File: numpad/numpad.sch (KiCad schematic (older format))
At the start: 13 parts, among them SW1 SW_PUSH, U1 ATMEGA32U4, X1 XTAL_GND

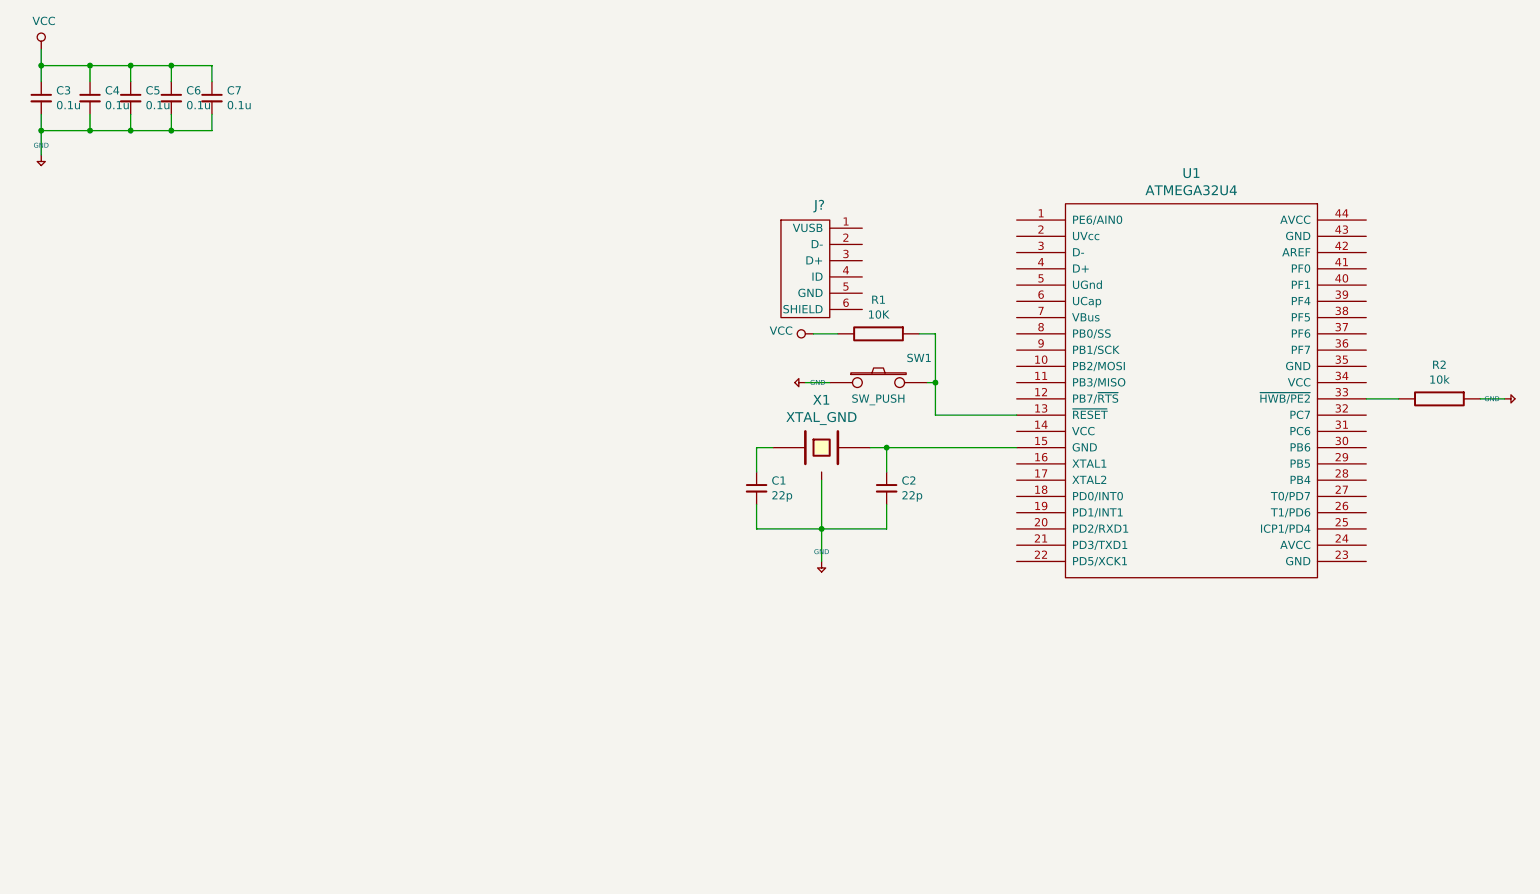
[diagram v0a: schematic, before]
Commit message: finished schematic, associated part to footprints
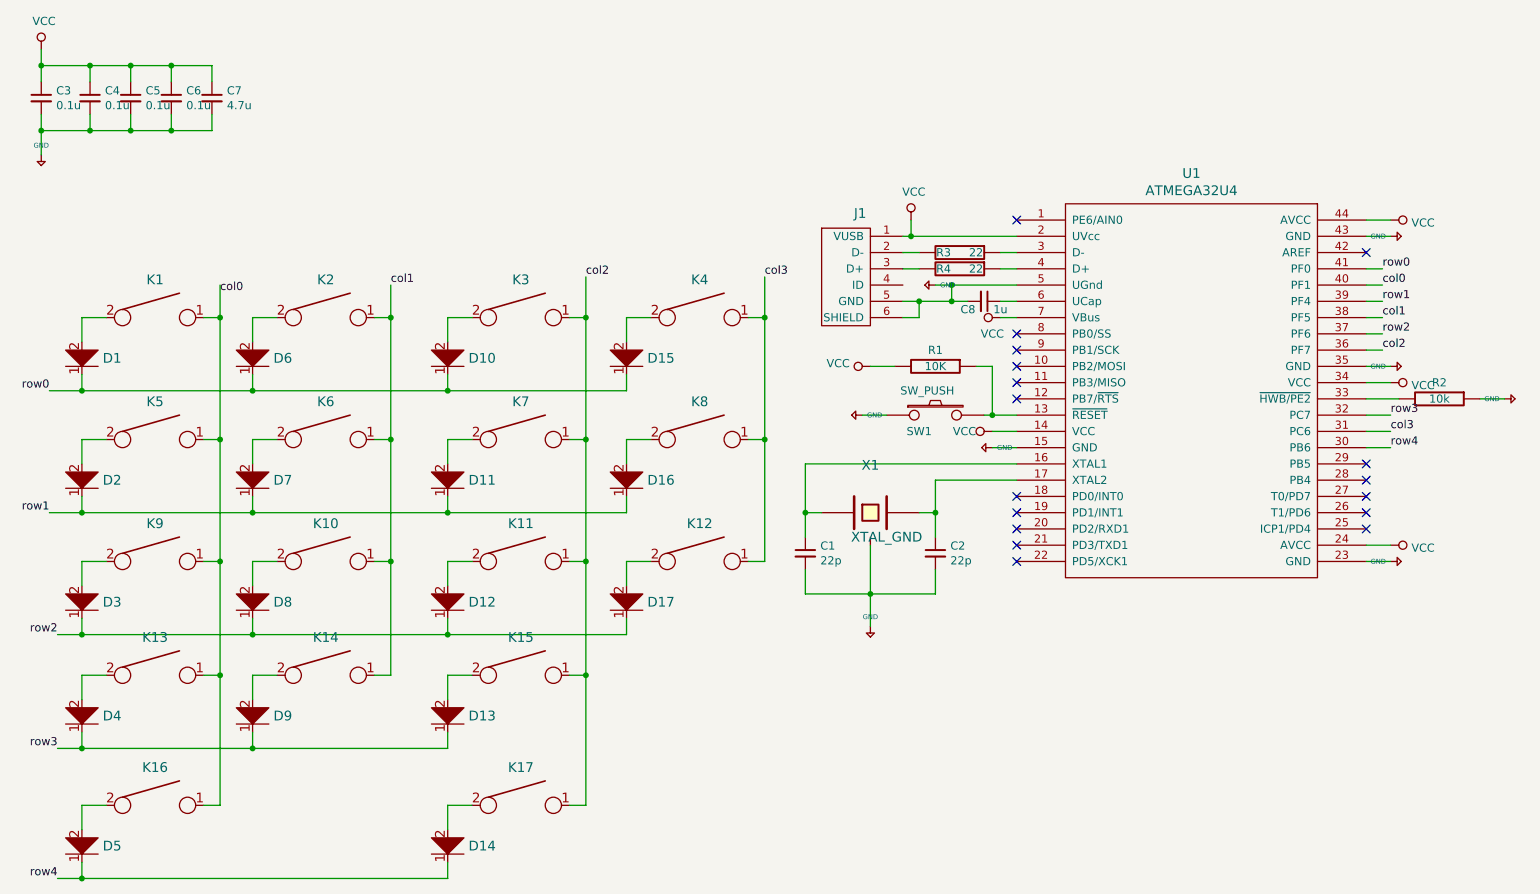
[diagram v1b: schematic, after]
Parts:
- added C8: 1u, Capacitor_SMD:C_0805_2012Metric_Pad1.15x1.40mm_HandSolder, symbol Device:C_Small
- added D1, D10, D11, D12, D13, D14, D15, D16, D17, D2, D3, D4, D5, D6, D7, D8, D9: D, keyboard_parts:D_SOD123_axial, symbol keyboard_parts:D
- added K1, K10, K11, K12, K13, K14, K15, K16, K17, K2, K3, K4, K5, K6, K7, K8, K9: KEYSW, keebs:Mx_Alps_100, symbol keyboard_parts:KEYSW
- added R3, R4: 22, Resistor_SMD:R_0805_2012Metric_Pad1.15x1.40mm_HandSolder, symbol keyboard_parts:R
- C1, C2, C3, C4, C5, C6: footprint (none) -> Capacitor_SMD:C_0805_2012Metric_Pad1.15x1.40mm_HandSolder
- C7: value 0.1u -> 4.7u; footprint (none) -> Capacitor_SMD:C_0805_2012Metric_Pad1.15x1.40mm_HandSolder
- J1: renamed from J?; footprint (none) -> keyboard_parts:USB_miniB_hirose_5S8
- R1, R2: footprint (none) -> Resistor_SMD:R_0805_2012Metric_Pad1.15x1.40mm_HandSolder
- SW1: footprint (none) -> Button_Switch_SMD:SW_SPST_TL3342
- U1: footprint (none) -> Package_QFP:TQFP-44_10x10mm_P0.8mm
- X1: footprint (none) -> Crystal:Crystal_SMD_SeikoEpson_FA238-4Pin_3.2x2.5mm_HandSoldering
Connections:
- net +5V: now also J1.5 (GND), J1.6 (SHIELD), U1.15 (GND), U1.23 (GND), U1.35 (GND), U1.43 (GND), U1.5 (UGnd), C8.2
- net VCC: now also J1.1 (VUSB), U1.14 (VCC), U1.2 (UVcc), U1.24 (AVCC), U1.34 (VCC), U1.44 (AVCC), U1.7 (VBus)
- net at C2.1, X1.3 (2): now also U1.17 (XTAL2); no longer U1.15 (GND)
- net at U1.16 (XTAL1): now also C1.1, X1.1
- net at U1.3 (D-): now also R3.1
- net row4: now reaches U1.30 (PB6)
- net row4: now also D14.1, D5.1
- net col3: now reaches U1.31 (PC6)
- net col3: now also K12.1, K4.1, K8.1
- net row3: now reaches U1.32 (PC7)
- net row3: now also D13.1, D4.1, D9.1
- net col2: now reaches U1.36 (PF7)
- net col2: now also K11.1, K15.1, K17.1, K3.1, K7.1
- net row2: now reaches U1.37 (PF6)
- net row2: now also D12.1, D17.1, D3.1, D8.1
- net col1: now reaches U1.38 (PF5)
- net col1: now also K10.1, K14.1, K2.1, K6.1
- net row1: now reaches U1.39 (PF4)
- net row1: now also D11.1, D16.1, D2.1, D7.1
- net at U1.4 (D+): now also R4.1
- net col0: now reaches U1.40 (PF1)
- net col0: now also K1.1, K13.1, K16.1, K5.1, K9.1
- net row0: now reaches U1.41 (PF0)
- net row0: now also D1.1, D10.1, D15.1, D6.1
- net at U1.6 (UCap): now also C8.1
- net at J1.2 (D-): now also R3.2
- net at J1.3 (D+): now also R4.2
- new net: D1.2, K1.2
- new net: D2.2, K5.2
- new net: D6.2, K2.2
- new net: D7.2, K6.2
- new net: D3.2, K9.2
- new net: D4.2, K13.2
- new net: D5.2, K16.2
- new net: D8.2, K10.2
- new net: D9.2, K14.2
- new net: D10.2, K3.2
- new net: D11.2, K7.2
- new net: D12.2, K11.2
- new net: D13.2, K15.2
- new net: D14.2, K17.2
- new net: D15.2, K4.2
- new net: D16.2, K8.2
- new net: D17.2, K12.2
- no-connect marks 0 -> 17
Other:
- moved on the sheet: C1, C2, J1, R1, SW1, X1

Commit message: finished initial pass on routing
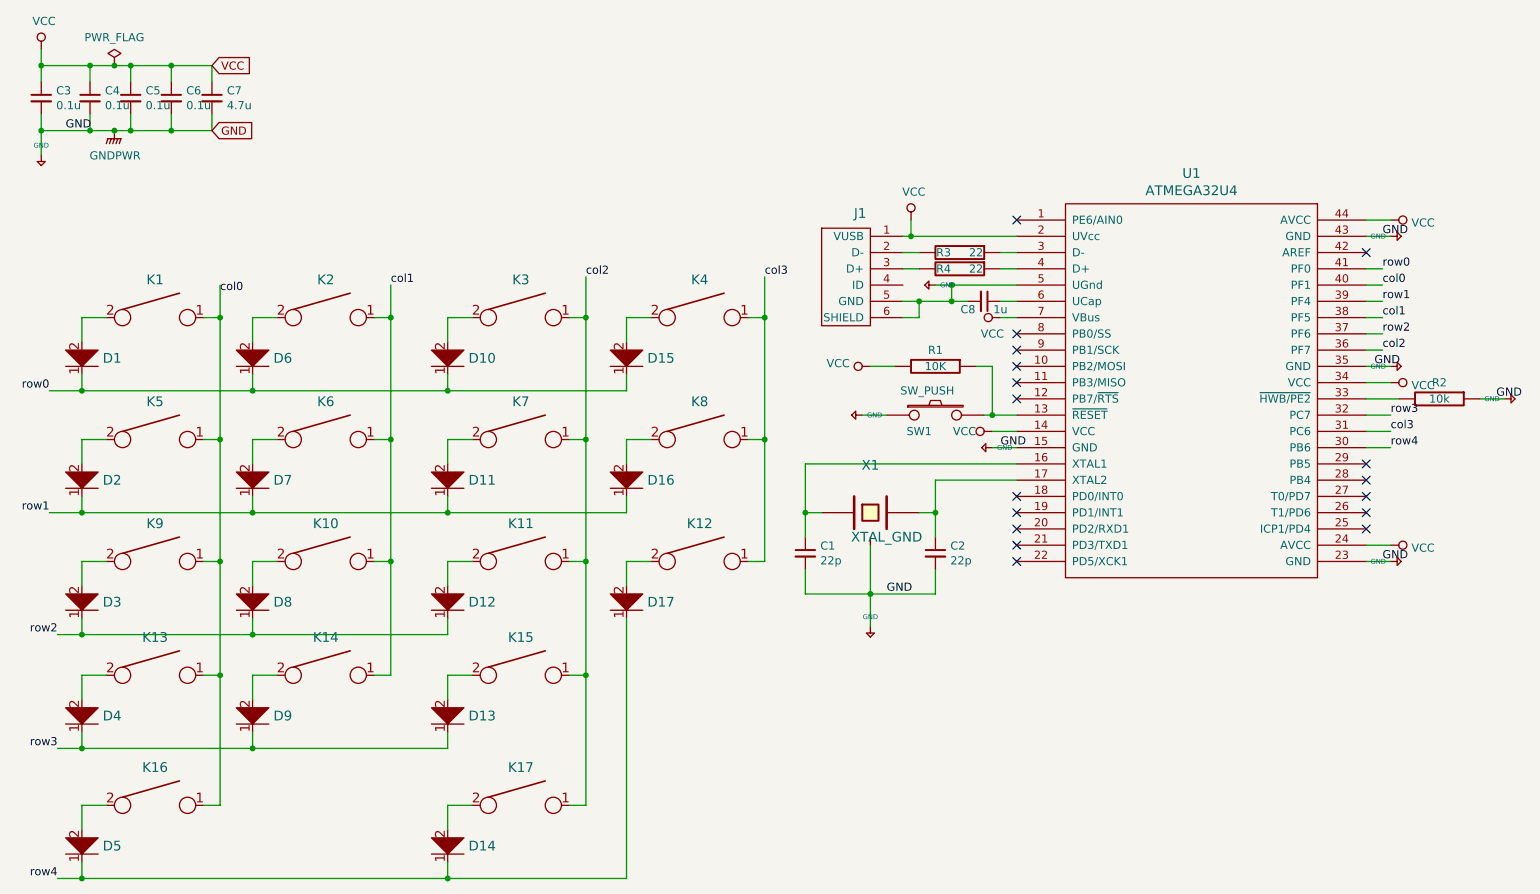
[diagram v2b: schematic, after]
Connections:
- net row2: no longer D17.1
- net row4: now also D17.1
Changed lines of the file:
@@
 $EndComp
-Wire Wire Line
-	6200 3750 6300 3750
-Wire Wire Line
-	6300 3900 6300 3750
-Wire Wire Line
-	5600 3750 5500 3750
-Wire Wire Line
-	5500 3750 5500 3900
 Wire Wire Line
 	5500 4100 5500 4250
@@
 Connection ~ 1100 1000
 Wire Wire Line
-	1100 1000 1350 1000
+	1100 1000 1250 1000
 Wire Wire Line
 	800  1300 800  1400
@@
 Connection ~ 1350 1400
 Wire Wire Line
-	1350 1400 1100 1400
+	1350 1400 1250 1400
 Wire Wire Line
 	1600 1300 1600 1400
@@
 	1    0    0    -1
 $EndComp
-Connection ~ 5500 3750
 $Comp
 L Device:C_Small C2
@@
 	1    0    0    -1
 $EndComp
-Wire Wire Line
-	5900 3950 5900 4250
 $Comp
 L keyboard_parts:XTAL_GND X1
@@
 	6800 3550 6300 3550
 Wire Wire Line
-	6300 3550 6300 3750
-Connection ~ 6300 3750
-Wire Wire Line
 	5500 3450 6800 3450
-Wire Wire Line
-	5500 3450 5500 3750
 Wire Wire Line
 	6650 3150 6800 3150
@@
 Wire Wire Line
 	1050 4500 2100 4500
-Wire Wire Line
-	4400 4400 4400 4500
 Connection ~ 2100 4500
 Wire Wire Line
@@
 	1050 4500 900  4500
 Connection ~ 1050 4500
-Wire Wire Line
-	3300 4500 4400 4500
-Connection ~ 3300 4500
 Wire Wire Line
 	5250 3300 5250 4050
@@
 NoConn ~ 6800 2650
 NoConn ~ 6800 1950
+Text Label 950  1400 0    50   ~ 0
+GND
+Text Label 6000 4250 0    50   ~ 0
+GND
+Text Label 6700 3350 0    50   ~ 0
+GND
+Text Label 9050 2050 0    50   ~ 0
+GND
+Text Label 9000 2850 0    50   ~ 0
+GND
+Text Label 9750 3050 0    50   ~ 0
+GND
+Text Label 9050 4050 0    50   ~ 0
+GND
+Text GLabel 1850 1400 2    50   Input ~ 0
+GND
+Text GLabel 1850 1000 2    50   Input ~ 0
+VCC
+Wire Wire Line
+	6300 3550 6300 3750
+Wire Wire Line
+	5500 3450 5500 3750
+Wire Wire Line
+	5600 3750 5500 3750
+Connection ~ 5500 3750
+Wire Wire Line
+	5500 3750 5500 3900
+Wire Wire Line
+	6200 3750 6300 3750
+Connection ~ 6300 3750
+Wire Wire Line
+	6300 3750 6300 3900
+Wire Wire Line
+	5900 3950 5900 4250
+$Comp
+L power:PWR_FLAG #FLG0101
+U 1 1 5F0A7EA2
+P 1250 1000
+F 0 "#FLG0101" H 1250 1075 50  0001 C CNN
+F 1 "PWR_FLAG" H 1250 1173 50  0000 C CNN
+F 2 "" H 1250 1000 50  0001 C CNN
+F 3 "~" H 1250 1000 50  0001 C CNN
+	1    1250 1000
+	1    0    0    -1
+$EndComp
+Connection ~ 1250 1000
+Wire Wire Line
+	1250 1000 1350 1000
+$Comp
+L power:GNDPWR #PWR0101
+U 1 1 5F0A922A
+P 1250 1400
+F 0 "#PWR0101" H 1250 1200 50  0001 C CNN
+F 1 "GNDPWR" H 1254 1246 50  0000 C CNN
+F 2 "" H 1250 1350 50  0001 C CNN
+F 3 "" H 1250 1350 50  0001 C CNN
+	1    1250 1400
+	1    0    0    -1
+$EndComp
+Connection ~ 1250 1400
+Wire Wire Line
+	1250 1400 1100 1400
+Wire Wire Line
+	4400 6000 3300 6000
+Wire Wire Line
+	4400 4400 4400 6000
+Connection ~ 3300 6000
 $EndSCHEMATC
